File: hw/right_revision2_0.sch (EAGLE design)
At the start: 64 parts, among them J2 CAN, X1 20MHz

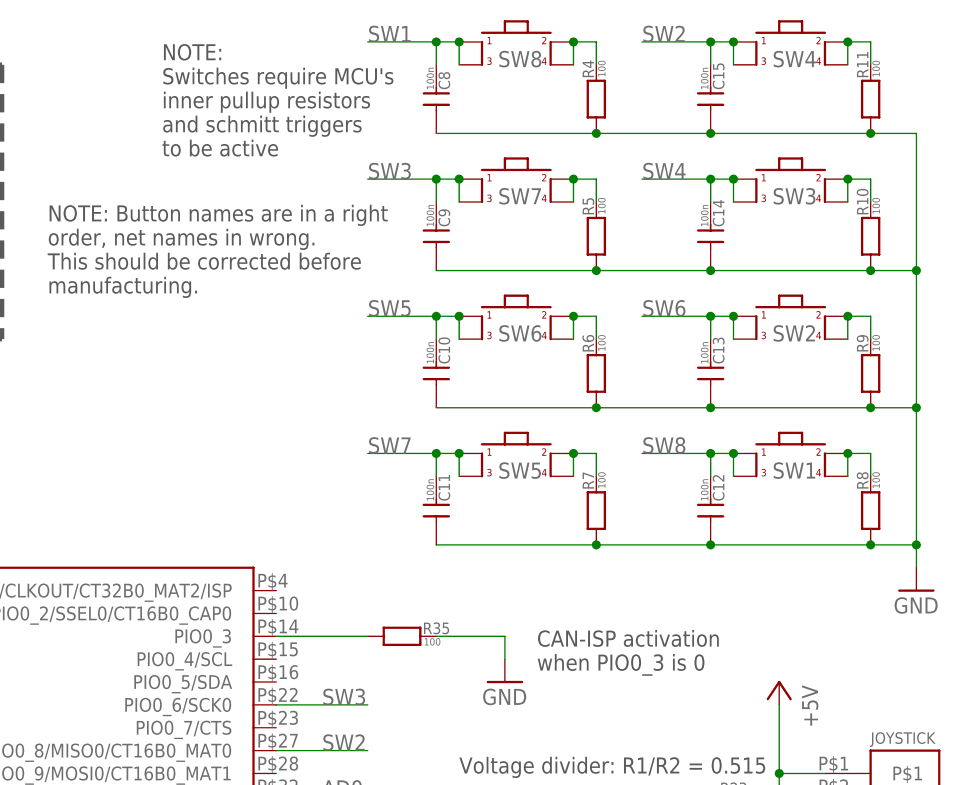
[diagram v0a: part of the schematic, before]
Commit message: Add 2.0 and 3.0 HW versions
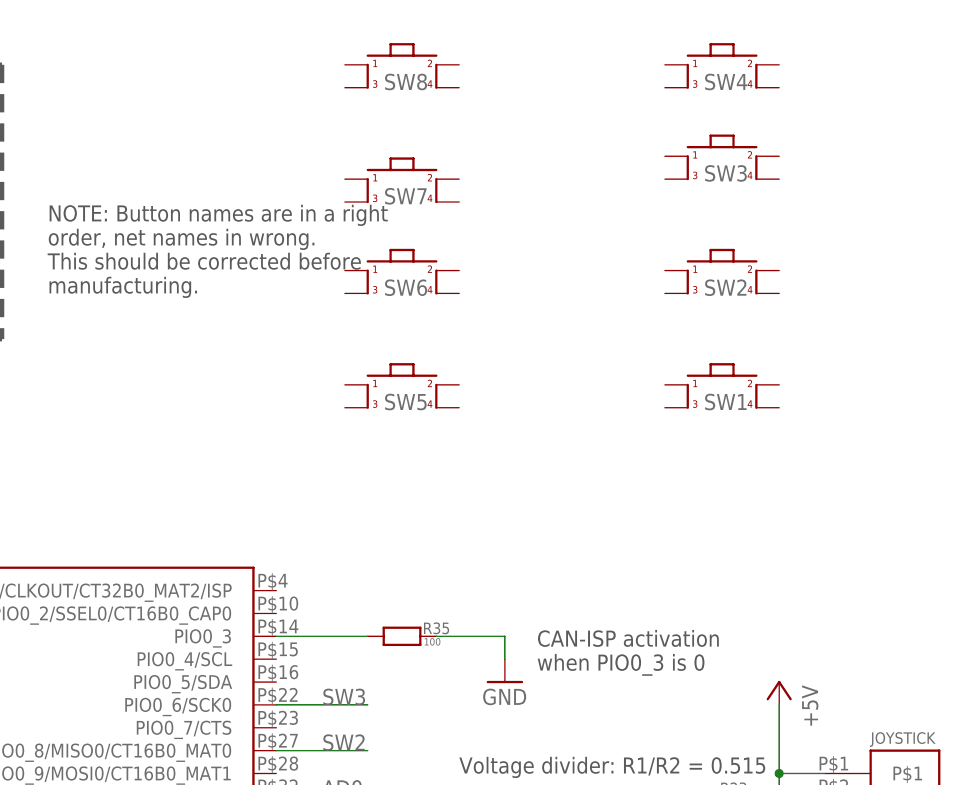
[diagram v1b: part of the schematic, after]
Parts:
- removed C10, C11, C12, C13, C14, C15, C8, C9: 100n, usevolt:CAP0603_SILKSCREEN
- removed R10, R11, R4, R5, R6, R7, R8, R9: 100, usevolt:RES0604_SILKSCREEN
- SW1, SW2, SW3, SW4, SW5, SW6, SW7, SW8: device arm:SWITCH12X12MM_CENTER_HOLE -> usevolt:SWITCH_EVQP6L
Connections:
- removed net N$12: R4.P$2, SW8.P$2, SW8.P$4
- removed net N$13: R5.P$2, SW7.P$2, SW7.P$4
- removed net N$14: R6.P$2, SW6.P$2, SW6.P$4
- removed net N$15: R11.P$2, SW4.P$2, SW4.P$4
- removed net N$16: R9.P$2, SW2.P$2, SW2.P$4
- removed net N$17: R10.P$2, SW3.P$2, SW3.P$4
- removed net N$18: R8.P$2, SW1.P$2, SW1.P$4
- removed net N$19: R7.P$2, SW5.P$2, SW5.P$4
- net GND: no longer C10.P$1, C11.P$1, C12.P$1, C13.P$1, C14.P$1, C15.P$1, C8.P$1, C9.P$1, R10.P$1, R11.P$1, R4.P$1, R5.P$1, R6.P$1, R7.P$1, R8.P$1, R9.P$1
- net SW1: no longer C8.P$2, SW8.P$1, SW8.P$3
- net SW2: no longer C15.P$2, SW4.P$1, SW4.P$3
- net SW3: no longer C9.P$2, SW7.P$1, SW7.P$3
- net SW4: no longer C14.P$2, SW3.P$1, SW3.P$3
- net SW5: no longer C10.P$2, SW6.P$1, SW6.P$3
- net SW6: no longer C13.P$2, SW2.P$1, SW2.P$3
- net SW7: no longer C11.P$2, SW5.P$1, SW5.P$3
- net SW8: no longer C12.P$2, SW1.P$1, SW1.P$3
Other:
- note removed: "NOTE: Switches require MCU's inner pullup resistors and schmitt triggers to be active"
- moved on the sheet: SW1, SW2, SW3, SW4, SW5, SW6, SW7, SW8
